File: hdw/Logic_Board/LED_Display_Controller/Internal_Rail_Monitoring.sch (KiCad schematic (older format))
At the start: 20 parts

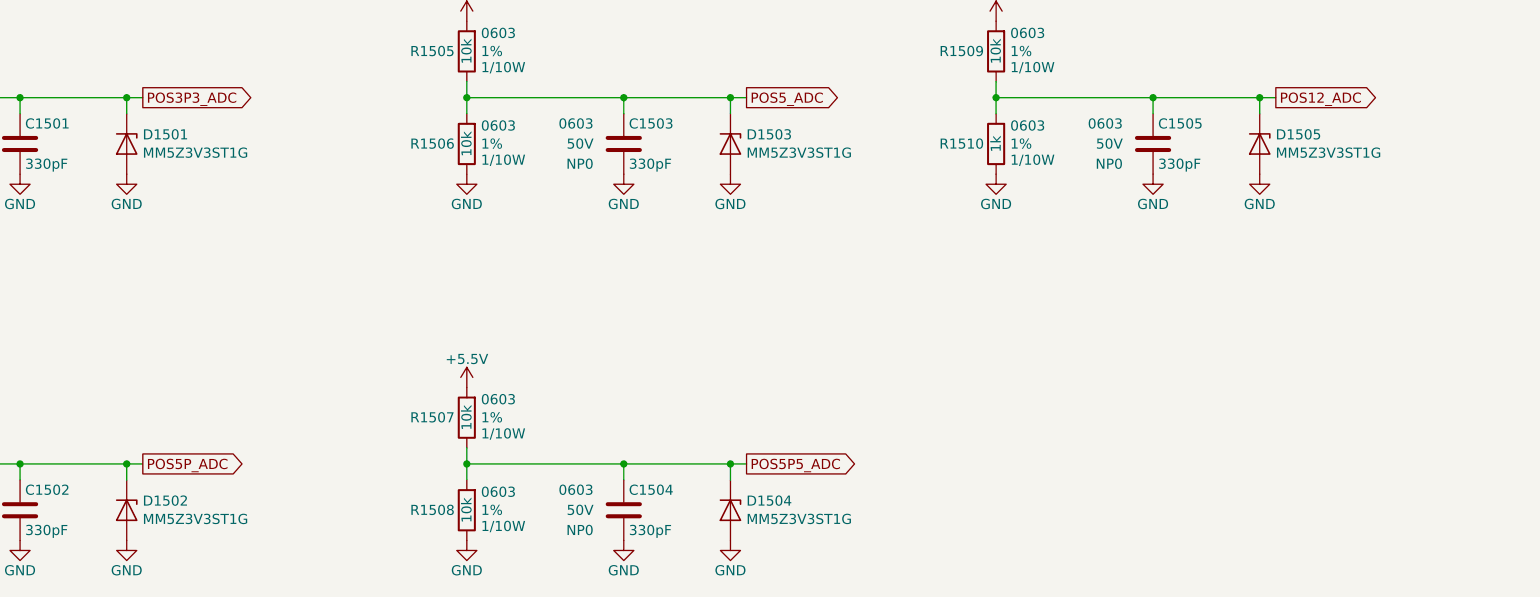
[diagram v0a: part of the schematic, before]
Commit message: Added some digikey partnumbers to components
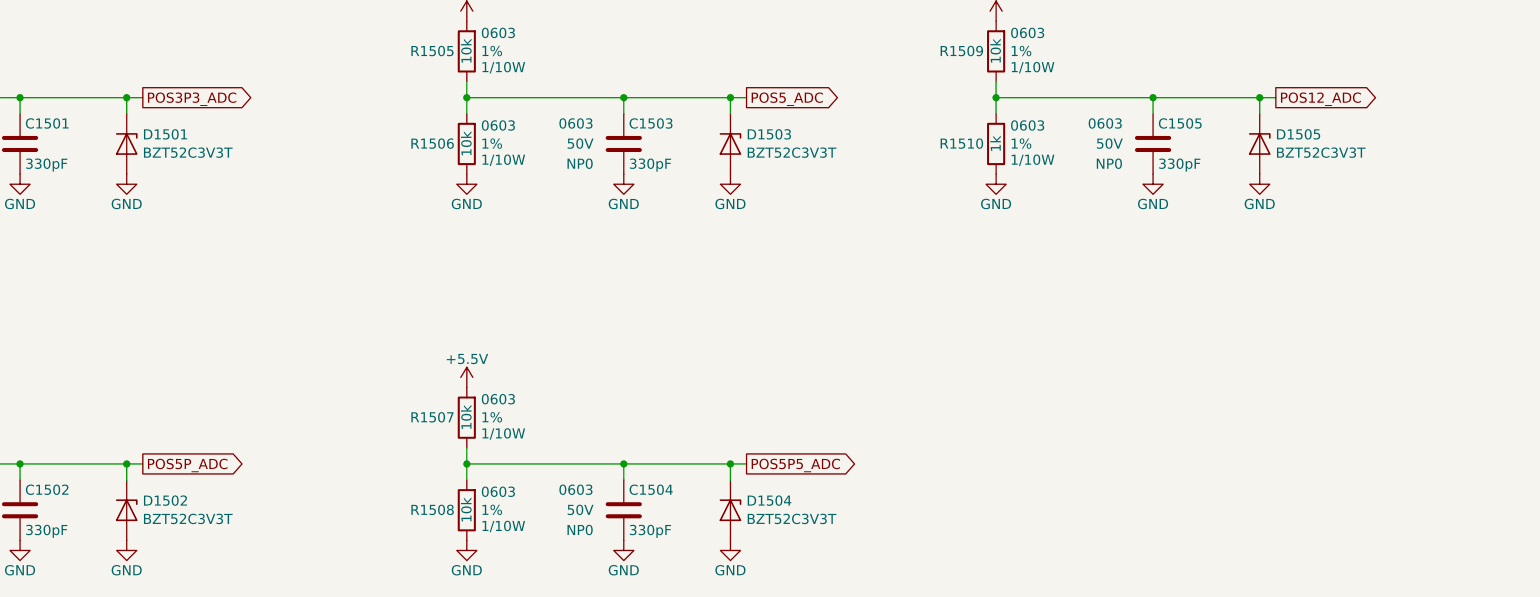
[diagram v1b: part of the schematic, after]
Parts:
- C1501, C1502, C1503, C1504, C1505: Digi-Key PN PN -> 399-6880-1-ND
- D1501, D1502, D1503, D1504, D1505: value MM5Z3V3ST1G -> BZT52C3V3T; Digi-Key PN (none) -> BZT52C3V3T-TPMSCT-ND
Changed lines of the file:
@@
 F 2 "" H 2328 3090 50  0001 C CNN
 F 3 "" H 2315 3340 50  0001 C CNN
-F 4 "PN" H 2715 3740 60  0001 C CNN "Digi-Key PN"
+F 4 "399-6880-1-ND" H 2715 3740 60  0001 C CNN "Digi-Key PN"
 F 5 "0603" H 2140 3340 50  0000 R CNN "display_footprint"
 F 6 "50V" H 2140 3240 50  0000 R CNN "Voltage"
@@
 P 2820 3240
 F 0 "D1501" V 2774 3319 50  0000 L CNN
-F 1 "MM5Z3V3ST1G" V 2865 3319 50  0000 L CNN
+F 1 "BZT52C3V3T" V 2865 3319 50  0000 L CNN
 F 2 "Diode_SMD:D_SOD-523" H 2820 3065 50  0001 C CNN
 F 3 "https://diotec.com/tl_files/diotec/files/pdf/datasheets/mm5z2v4.pdf" H 2820 3240 50  0001 C CNN
+F 4 "BZT52C3V3T-TPMSCT-ND" H 0   0   50  0001 C CNN "Digi-Key PN"
 	1    2820 3240
 	0    1    1    0
@@
 F 2 "" H 5328 3090 50  0001 C CNN
 F 3 "" H 5315 3340 50  0001 C CNN
-F 4 "PN" H 5715 3740 60  0001 C CNN "Digi-Key PN"
+F 4 "399-6880-1-ND" H 5715 3740 60  0001 C CNN "Digi-Key PN"
 F 5 "0603" H 5140 3340 50  0000 R CNN "display_footprint"
 F 6 "50V" H 5140 3240 50  0000 R CNN "Voltage"
@@
 P 5820 3240
 F 0 "D1503" V 5774 3319 50  0000 L CNN
-F 1 "MM5Z3V3ST1G" V 5865 3319 50  0000 L CNN
+F 1 "BZT52C3V3T" V 5865 3319 50  0000 L CNN
 F 2 "Diode_SMD:D_SOD-523" H 5820 3065 50  0001 C CNN
 F 3 "https://diotec.com/tl_files/diotec/files/pdf/datasheets/mm5z2v4.pdf" H 5820 3240 50  0001 C CNN
+F 4 "BZT52C3V3T-TPMSCT-ND" H 0   0   50  0001 C CNN "Digi-Key PN"
 	1    5820 3240
 	0    1    1    0
@@
 F 2 "" H 7958 3090 50  0001 C CNN
 F 3 "" H 7945 3340 50  0001 C CNN
-F 4 "PN" H 8345 3740 60  0001 C CNN "Digi-Key PN"
+F 4 "399-6880-1-ND" H 8345 3740 60  0001 C CNN "Digi-Key PN"
 F 5 "0603" H 7770 3340 50  0000 R CNN "display_footprint"
 F 6 "50V" H 7770 3240 50  0000 R CNN "Voltage"
@@
 P 8450 3240
 F 0 "D1505" V 8404 3319 50  0000 L CNN
-F 1 "MM5Z3V3ST1G" V 8495 3319 50  0000 L CNN
+F 1 "BZT52C3V3T" V 8495 3319 50  0000 L CNN
 F 2 "Diode_SMD:D_SOD-523" H 8450 3065 50  0001 C CNN
 F 3 "https://diotec.com/tl_files/diotec/files/pdf/datasheets/mm5z2v4.pdf" H 8450 3240 50  0001 C CNN
+F 4 "BZT52C3V3T-TPMSCT-ND" H 0   0   50  0001 C CNN "Digi-Key PN"
 	1    8450 3240
 	0    1    1    0
@@
 F 2 "" H 2328 4910 50  0001 C CNN
 F 3 "" H 2315 5160 50  0001 C CNN
-F 4 "PN" H 2715 5560 60  0001 C CNN "Digi-Key PN"
+F 4 "399-6880-1-ND" H 2715 5560 60  0001 C CNN "Digi-Key PN"
 F 5 "0603" H 2140 5160 50  0000 R CNN "display_footprint"
 F 6 "50V" H 2140 5060 50  0000 R CNN "Voltage"
@@
 P 2820 5060
 F 0 "D1502" V 2774 5139 50  0000 L CNN
-F 1 "MM5Z3V3ST1G" V 2865 5139 50  0000 L CNN
+F 1 "BZT52C3V3T" V 2865 5139 50  0000 L CNN
 F 2 "Diode_SMD:D_SOD-523" H 2820 4885 50  0001 C CNN
 F 3 "https://diotec.com/tl_files/diotec/files/pdf/datasheets/mm5z2v4.pdf" H 2820 5060 50  0001 C CNN
+F 4 "BZT52C3V3T-TPMSCT-ND" H 0   0   50  0001 C CNN "Digi-Key PN"
 	1    2820 5060
 	0    1    1    0
@@
 F 2 "" H 5328 4910 50  0001 C CNN
 F 3 "" H 5315 5160 50  0001 C CNN
-F 4 "PN" H 5715 5560 60  0001 C CNN "Digi-Key PN"
+F 4 "399-6880-1-ND" H 5715 5560 60  0001 C CNN "Digi-Key PN"
 F 5 "0603" H 5140 5160 50  0000 R CNN "display_footprint"
 F 6 "50V" H 5140 5060 50  0000 R CNN "Voltage"
@@
 P 5820 5060
 F 0 "D1504" V 5774 5139 50  0000 L CNN
-F 1 "MM5Z3V3ST1G" V 5865 5139 50  0000 L CNN
+F 1 "BZT52C3V3T" V 5865 5139 50  0000 L CNN
 F 2 "Diode_SMD:D_SOD-523" H 5820 4885 50  0001 C CNN
 F 3 "https://diotec.com/tl_files/diotec/files/pdf/datasheets/mm5z2v4.pdf" H 5820 5060 50  0001 C CNN
+F 4 "BZT52C3V3T-TPMSCT-ND" H 0   0   50  0001 C CNN "Digi-Key PN"
 	1    5820 5060
 	0    1    1    0

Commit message: Finished first pass of digikey part numbers
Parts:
- R1501, R1502, R1503, R1504, R1505, R1506, R1507, R1508, R1509: Digi-Key PN PN -> RMCF0603FT10K0CT-ND
- R1510: Digi-Key PN PN -> RMCF0603FT1K00CT-ND
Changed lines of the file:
@@
 F 5 "1%" H 1580 2780 50  0000 L CNN "Tolerance"
 F 6 "1/10W" H 1580 2700 50  0000 L CNN "Wattage"
-F 7 "PN" H 1810 3180 60  0001 C CNN "Digi-Key PN"
+F 7 "RMCF0603FT10K0CT-ND" H 1810 3180 60  0001 C CNN "Digi-Key PN"
 	1    1510 2780
 	1    0    0    -1
@@
 F 5 "1%" H 1580 3240 50  0000 L CNN "Tolerance"
 F 6 "1/10W" H 1580 3160 50  0000 L CNN "Wattage"
-F 7 "PN" H 1810 3640 60  0001 C CNN "Digi-Key PN"
+F 7 "RMCF0603FT10K0CT-ND" H 1810 3640 60  0001 C CNN "Digi-Key PN"
 	1    1510 3240
 	1    0    0    -1
@@
 F 5 "1%" H 4580 2780 50  0000 L CNN "Tolerance"
 F 6 "1/10W" H 4580 2700 50  0000 L CNN "Wattage"
-F 7 "PN" H 4810 3180 60  0001 C CNN "Digi-Key PN"
+F 7 "RMCF0603FT10K0CT-ND" H 4810 3180 60  0001 C CNN "Digi-Key PN"
 	1    4510 2780
 	1    0    0    -1
@@
 F 5 "1%" H 4580 3240 50  0000 L CNN "Tolerance"
 F 6 "1/10W" H 4580 3160 50  0000 L CNN "Wattage"
-F 7 "PN" H 4810 3640 60  0001 C CNN "Digi-Key PN"
+F 7 "RMCF0603FT10K0CT-ND" H 4810 3640 60  0001 C CNN "Digi-Key PN"
 	1    4510 3240
 	1    0    0    -1
@@
 F 5 "1%" H 7210 2780 50  0000 L CNN "Tolerance"
 F 6 "1/10W" H 7210 2700 50  0000 L CNN "Wattage"
-F 7 "PN" H 7440 3180 60  0001 C CNN "Digi-Key PN"
+F 7 "RMCF0603FT10K0CT-ND" H 7440 3180 60  0001 C CNN "Digi-Key PN"
 	1    7140 2780
 	1    0    0    -1
@@
 F 5 "1%" H 7210 3240 50  0000 L CNN "Tolerance"
 F 6 "1/10W" H 7210 3160 50  0000 L CNN "Wattage"
-F 7 "PN" H 7440 3640 60  0001 C CNN "Digi-Key PN"
+F 7 "RMCF0603FT1K00CT-ND" H 7440 3640 60  0001 C CNN "Digi-Key PN"
 	1    7140 3240
 	1    0    0    -1
@@
 F 5 "1%" H 1580 4600 50  0000 L CNN "Tolerance"
 F 6 "1/10W" H 1580 4520 50  0000 L CNN "Wattage"
-F 7 "PN" H 1810 5000 60  0001 C CNN "Digi-Key PN"
+F 7 "RMCF0603FT10K0CT-ND" H 1810 5000 60  0001 C CNN "Digi-Key PN"
 	1    1510 4600
 	1    0    0    -1
@@
 F 5 "1%" H 1580 5060 50  0000 L CNN "Tolerance"
 F 6 "1/10W" H 1580 4980 50  0000 L CNN "Wattage"
-F 7 "PN" H 1810 5460 60  0001 C CNN "Digi-Key PN"
+F 7 "RMCF0603FT10K0CT-ND" H 1810 5460 60  0001 C CNN "Digi-Key PN"
 	1    1510 5060
 	1    0    0    -1
@@
 F 5 "1%" H 4580 4600 50  0000 L CNN "Tolerance"
 F 6 "1/10W" H 4580 4520 50  0000 L CNN "Wattage"
-F 7 "PN" H 4810 5000 60  0001 C CNN "Digi-Key PN"
+F 7 "RMCF0603FT10K0CT-ND" H 4810 5000 60  0001 C CNN "Digi-Key PN"
 	1    4510 4600
 	1    0    0    -1
@@
 F 5 "1%" H 4580 5060 50  0000 L CNN "Tolerance"
 F 6 "1/10W" H 4580 4980 50  0000 L CNN "Wattage"
-F 7 "PN" H 4810 5460 60  0001 C CNN "Digi-Key PN"
+F 7 "RMCF0603FT10K0CT-ND" H 4810 5460 60  0001 C CNN "Digi-Key PN"
 	1    4510 5060
 	1    0    0    -1

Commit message: First pass assignment of footprints to all components
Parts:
- C1501, C1502, C1503, C1504, C1505: footprint (none) -> Capacitors_SMD:C_0603
- D1501, D1502, D1503, D1504, D1505: footprint Diode_SMD:D_SOD-523 -> Diodes_SMD:D_SOD-523
- R1501, R1502, R1503, R1504, R1505, R1506, R1507, R1508, R1509, R1510: footprint (none) -> Resistors_SMD:R_0603
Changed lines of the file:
@@
 F 0 "R1501" H 1450 2780 50  0000 R CNN
 F 1 "10k" V 1510 2780 50  0000 C CNN
-F 2 "" H 1510 2780 50  0001 C CNN
+F 2 "Resistors_SMD:R_0603" H 1510 2780 50  0001 C CNN
 F 3 "" H 1510 2780 50  0001 C CNN
 F 4 "0603" H 1580 2870 50  0000 L CNN "display_footprint"
@@
 F 0 "R1502" H 1450 3240 50  0000 R CNN
 F 1 "10k" V 1510 3240 50  0000 C CNN
-F 2 "" H 1510 3240 50  0001 C CNN
+F 2 "Resistors_SMD:R_0603" H 1510 3240 50  0001 C CNN
 F 3 "" H 1510 3240 50  0001 C CNN
 F 4 "0603" H 1580 3330 50  0000 L CNN "display_footprint"
@@
 F 0 "C1501" H 2315 3340 50  0000 L CNN
 F 1 "330pF" H 2315 3140 50  0000 L CNN
-F 2 "" H 2328 3090 50  0001 C CNN
+F 2 "Capacitors_SMD:C_0603" H 2328 3090 50  0001 C CNN
 F 3 "" H 2315 3340 50  0001 C CNN
 F 4 "399-6880-1-ND" H 2715 3740 60  0001 C CNN "Digi-Key PN"
@@
 F 0 "D1501" V 2774 3319 50  0000 L CNN
 F 1 "BZT52C3V3T" V 2865 3319 50  0000 L CNN
-F 2 "Diode_SMD:D_SOD-523" H 2820 3065 50  0001 C CNN
+F 2 "Diodes_SMD:D_SOD-523" H 2820 3065 50  0001 C CNN
 F 3 "https://diotec.com/tl_files/diotec/files/pdf/datasheets/mm5z2v4.pdf" H 2820 3240 50  0001 C CNN
 F 4 "BZT52C3V3T-TPMSCT-ND" H 0   0   50  0001 C CNN "Digi-Key PN"
@@
 F 0 "R1505" H 4450 2780 50  0000 R CNN
 F 1 "10k" V 4510 2780 50  0000 C CNN
-F 2 "" H 4510 2780 50  0001 C CNN
+F 2 "Resistors_SMD:R_0603" H 4510 2780 50  0001 C CNN
 F 3 "" H 4510 2780 50  0001 C CNN
 F 4 "0603" H 4580 2870 50  0000 L CNN "display_footprint"
@@
 F 0 "R1506" H 4450 3240 50  0000 R CNN
 F 1 "10k" V 4510 3240 50  0000 C CNN
-F 2 "" H 4510 3240 50  0001 C CNN
+F 2 "Resistors_SMD:R_0603" H 4510 3240 50  0001 C CNN
 F 3 "" H 4510 3240 50  0001 C CNN
 F 4 "0603" H 4580 3330 50  0000 L CNN "display_footprint"
@@
 F 0 "C1503" H 5315 3340 50  0000 L CNN
 F 1 "330pF" H 5315 3140 50  0000 L CNN
-F 2 "" H 5328 3090 50  0001 C CNN
+F 2 "Capacitors_SMD:C_0603" H 5328 3090 50  0001 C CNN
 F 3 "" H 5315 3340 50  0001 C CNN
 F 4 "399-6880-1-ND" H 5715 3740 60  0001 C CNN "Digi-Key PN"
@@
 F 0 "D1503" V 5774 3319 50  0000 L CNN
 F 1 "BZT52C3V3T" V 5865 3319 50  0000 L CNN
-F 2 "Diode_SMD:D_SOD-523" H 5820 3065 50  0001 C CNN
+F 2 "Diodes_SMD:D_SOD-523" H 5820 3065 50  0001 C CNN
 F 3 "https://diotec.com/tl_files/diotec/files/pdf/datasheets/mm5z2v4.pdf" H 5820 3240 50  0001 C CNN
 F 4 "BZT52C3V3T-TPMSCT-ND" H 0   0   50  0001 C CNN "Digi-Key PN"
@@
 F 0 "R1509" H 7080 2780 50  0000 R CNN
 F 1 "10k" V 7140 2780 50  0000 C CNN
-F 2 "" H 7140 2780 50  0001 C CNN
+F 2 "Resistors_SMD:R_0603" H 7140 2780 50  0001 C CNN
 F 3 "" H 7140 2780 50  0001 C CNN
 F 4 "0603" H 7210 2870 50  0000 L CNN "display_footprint"
@@
 F 0 "R1510" H 7080 3240 50  0000 R CNN
 F 1 "1k" V 7140 3240 50  0000 C CNN
-F 2 "" H 7140 3240 50  0001 C CNN
+F 2 "Resistors_SMD:R_0603" H 7140 3240 50  0001 C CNN
 F 3 "" H 7140 3240 50  0001 C CNN
 F 4 "0603" H 7210 3330 50  0000 L CNN "display_footprint"
@@
 F 0 "C1505" H 7945 3340 50  0000 L CNN
 F 1 "330pF" H 7945 3140 50  0000 L CNN
-F 2 "" H 7958 3090 50  0001 C CNN
+F 2 "Capacitors_SMD:C_0603" H 7958 3090 50  0001 C CNN
 F 3 "" H 7945 3340 50  0001 C CNN
 F 4 "399-6880-1-ND" H 8345 3740 60  0001 C CNN "Digi-Key PN"
@@
 F 0 "D1505" V 8404 3319 50  0000 L CNN
 F 1 "BZT52C3V3T" V 8495 3319 50  0000 L CNN
-F 2 "Diode_SMD:D_SOD-523" H 8450 3065 50  0001 C CNN
+F 2 "Diodes_SMD:D_SOD-523" H 8450 3065 50  0001 C CNN
 F 3 "https://diotec.com/tl_files/diotec/files/pdf/datasheets/mm5z2v4.pdf" H 8450 3240 50  0001 C CNN
 F 4 "BZT52C3V3T-TPMSCT-ND" H 0   0   50  0001 C CNN "Digi-Key PN"
@@
 F 0 "R1503" H 1450 4600 50  0000 R CNN
 F 1 "10k" V 1510 4600 50  0000 C CNN
-F 2 "" H 1510 4600 50  0001 C CNN
+F 2 "Resistors_SMD:R_0603" H 1510 4600 50  0001 C CNN
 F 3 "" H 1510 4600 50  0001 C CNN
 F 4 "0603" H 1580 4690 50  0000 L CNN "display_footprint"
@@
 F 0 "R1504" H 1450 5060 50  0000 R CNN
 F 1 "10k" V 1510 5060 50  0000 C CNN
-F 2 "" H 1510 5060 50  0001 C CNN
+F 2 "Resistors_SMD:R_0603" H 1510 5060 50  0001 C CNN
 F 3 "" H 1510 5060 50  0001 C CNN
 F 4 "0603" H 1580 5150 50  0000 L CNN "display_footprint"
@@
 F 0 "C1502" H 2315 5160 50  0000 L CNN
 F 1 "330pF" H 2315 4960 50  0000 L CNN
-F 2 "" H 2328 4910 50  0001 C CNN
+F 2 "Capacitors_SMD:C_0603" H 2328 4910 50  0001 C CNN
 F 3 "" H 2315 5160 50  0001 C CNN
 F 4 "399-6880-1-ND" H 2715 5560 60  0001 C CNN "Digi-Key PN"
@@
 F 0 "D1502" V 2774 5139 50  0000 L CNN
 F 1 "BZT52C3V3T" V 2865 5139 50  0000 L CNN
-F 2 "Diode_SMD:D_SOD-523" H 2820 4885 50  0001 C CNN
+F 2 "Diodes_SMD:D_SOD-523" H 2820 4885 50  0001 C CNN
 F 3 "https://diotec.com/tl_files/diotec/files/pdf/datasheets/mm5z2v4.pdf" H 2820 5060 50  0001 C CNN
 F 4 "BZT52C3V3T-TPMSCT-ND" H 0   0   50  0001 C CNN "Digi-Key PN"
@@
 F 0 "R1507" H 4450 4600 50  0000 R CNN
 F 1 "10k" V 4510 4600 50  0000 C CNN
-F 2 "" H 4510 4600 50  0001 C CNN
+F 2 "Resistors_SMD:R_0603" H 4510 4600 50  0001 C CNN
 F 3 "" H 4510 4600 50  0001 C CNN
 F 4 "0603" H 4580 4690 50  0000 L CNN "display_footprint"
@@
 F 0 "R1508" H 4450 5060 50  0000 R CNN
 F 1 "10k" V 4510 5060 50  0000 C CNN
-F 2 "" H 4510 5060 50  0001 C CNN
+F 2 "Resistors_SMD:R_0603" H 4510 5060 50  0001 C CNN
 F 3 "" H 4510 5060 50  0001 C CNN
 F 4 "0603" H 4580 5150 50  0000 L CNN "display_footprint"
@@
 F 0 "C1504" H 5315 5160 50  0000 L CNN
 F 1 "330pF" H 5315 4960 50  0000 L CNN
-F 2 "" H 5328 4910 50  0001 C CNN
+F 2 "Capacitors_SMD:C_0603" H 5328 4910 50  0001 C CNN
 F 3 "" H 5315 5160 50  0001 C CNN
 F 4 "399-6880-1-ND" H 5715 5560 60  0001 C CNN "Digi-Key PN"
@@
 F 0 "D1504" V 5774 5139 50  0000 L CNN
 F 1 "BZT52C3V3T" V 5865 5139 50  0000 L CNN
-F 2 "Diode_SMD:D_SOD-523" H 5820 4885 50  0001 C CNN
+F 2 "Diodes_SMD:D_SOD-523" H 5820 4885 50  0001 C CNN
 F 3 "https://diotec.com/tl_files/diotec/files/pdf/datasheets/mm5z2v4.pdf" H 5820 5060 50  0001 C CNN
 F 4 "BZT52C3V3T-TPMSCT-ND" H 0   0   50  0001 C CNN "Digi-Key PN"

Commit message: Resolved a few library dependencies
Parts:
- R1501, R1502, R1503, R1504, R1505, R1506, R1507, R1508, R1509, R1510: symbol Custom_Library:R_Custom -> LED_Display_Local_Library:R_Custom
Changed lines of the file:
@@
 $EndDescr
 $Comp
-L Custom_Library:R_Custom R?
+L LED_Display_Local_Library:R_Custom R?
 U 1 1 5BEF531C
 P 1510 2780
@@
 $EndComp
 $Comp
-L Custom_Library:R_Custom R?
+L LED_Display_Local_Library:R_Custom R?
 U 1 1 5BEF532E
 P 1510 3240
@@
 Connection ~ 2820 3010
 $Comp
-L Custom_Library:R_Custom R?
+L LED_Display_Local_Library:R_Custom R?
 U 1 1 5BF09C2E
 P 4510 2780
@@
 $EndComp
 $Comp
-L Custom_Library:R_Custom R?
+L LED_Display_Local_Library:R_Custom R?
 U 1 1 5BF09C39
 P 4510 3240
@@
 $EndComp
 $Comp
-L Custom_Library:R_Custom R?
+L LED_Display_Local_Library:R_Custom R?
 U 1 1 5BF0BD4E
 P 7140 2780
@@
 $EndComp
 $Comp
-L Custom_Library:R_Custom R?
+L LED_Display_Local_Library:R_Custom R?
 U 1 1 5BF0BD59
 P 7140 3240
@@
 $EndComp
 $Comp
-L Custom_Library:R_Custom R?
+L LED_Display_Local_Library:R_Custom R?
 U 1 1 5BF18632
 P 1510 4600
@@
 $EndComp
 $Comp
-L Custom_Library:R_Custom R?
+L LED_Display_Local_Library:R_Custom R?
 U 1 1 5BF1863D
 P 1510 5060
@@
 Connection ~ 2820 4830
 $Comp
-L Custom_Library:R_Custom R?
+L LED_Display_Local_Library:R_Custom R?
 U 1 1 5BF1867D
 P 4510 4600
@@
 $EndComp
 $Comp
-L Custom_Library:R_Custom R?
+L LED_Display_Local_Library:R_Custom R?
 U 1 1 5BF18688
 P 4510 5060
@@
 $EndComp
 $Comp
-L Custom_Library:+5.5V #PWR01511
+L LED_Display_Local_Library:+5.5V #PWR01511
 U 1 1 5BF18F83
 P 4510 4450
